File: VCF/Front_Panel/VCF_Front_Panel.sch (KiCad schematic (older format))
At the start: 1 part

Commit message: Bunch of bug fixes and tweaks
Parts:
- removed TP1: TestPoint, TestPoint:TestPoint_Pad_1.0x1.0mm, symbol Connector:TestPoint
- added H1: Top_MH, Eurorack:eurorack_mounting_hole, symbol Mechanical:MountingHole_Pad
- added H10: Res_Amt, Eurorack:pot_fp_hole, symbol Mechanical:MountingHole_Pad
- added H11: Res_Mod, Eurorack:jack_fp_hole, symbol Mechanical:MountingHole_Pad
- added H12: In_1, Eurorack:jack_fp_hole, symbol Mechanical:MountingHole_Pad
- added H13: In_2, Eurorack:jack_fp_hole, symbol Mechanical:MountingHole_Pad
- added H14: In_3, Eurorack:jack_fp_hole, symbol Mechanical:MountingHole_Pad
- added H15: Out, Eurorack:jack_fp_hole, symbol Mechanical:MountingHole_Pad
- added H2: Cutoff, Eurorack:pot_fp_hole, symbol Mechanical:MountingHole_Pad
- added H3: Cutoff_Amt, Eurorack:pot_fp_hole, symbol Mechanical:MountingHole_Pad
- added H4: Cutoff_Mod, Eurorack:jack_fp_hole, symbol Mechanical:MountingHole_Pad
- added H5: In_Amt_1, Eurorack:pot_fp_hole, symbol Mechanical:MountingHole_Pad
- added H6: In_Amt_2, Eurorack:pot_fp_hole, symbol Mechanical:MountingHole_Pad
- added H7: In_Amt_3, Eurorack:pot_fp_hole, symbol Mechanical:MountingHole_Pad
- added H8: Bottom_MH, Eurorack:eurorack_mounting_hole, symbol Mechanical:MountingHole_Pad
- added H9: Res, Eurorack:pot_fp_hole, symbol Mechanical:MountingHole_Pad
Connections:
- wire segments 2 -> 0

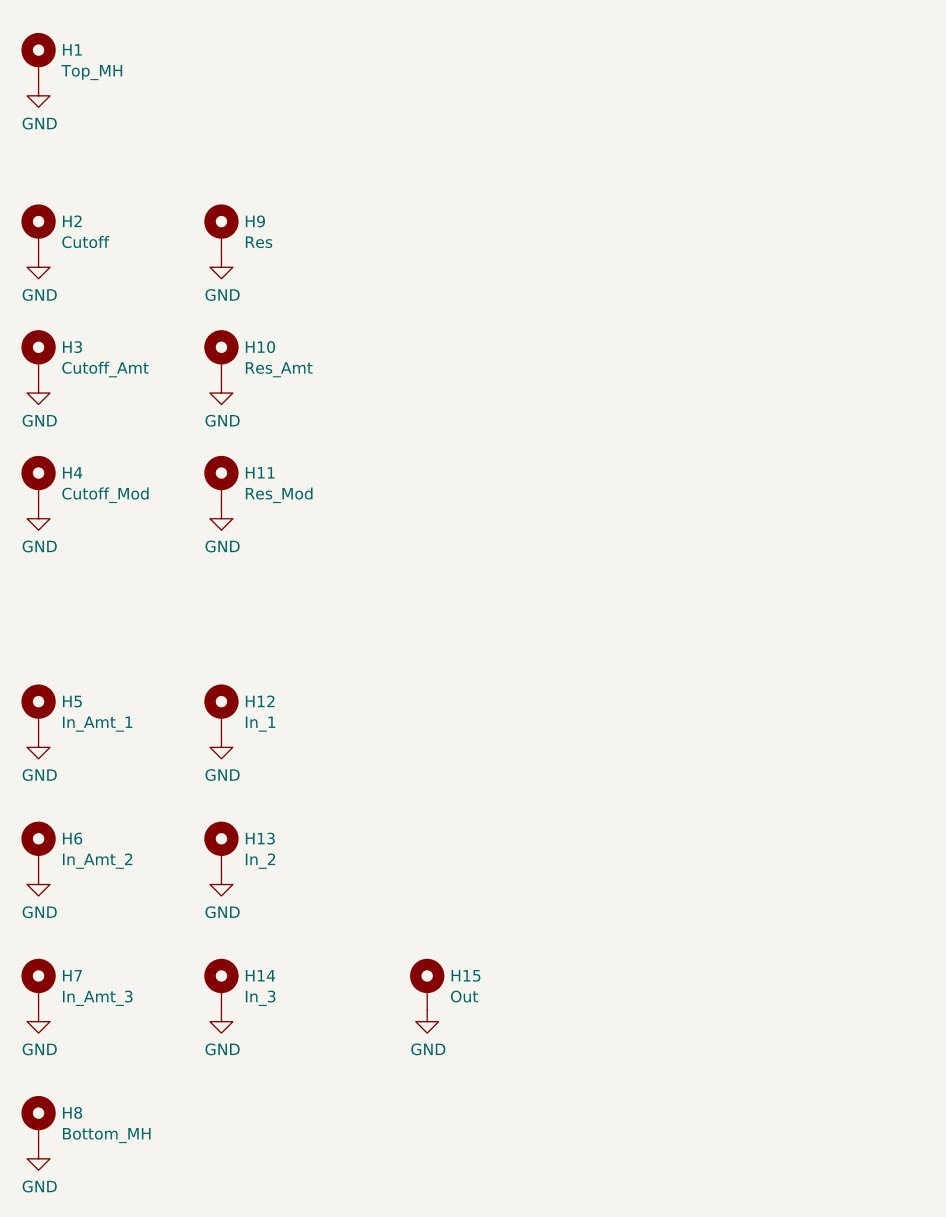
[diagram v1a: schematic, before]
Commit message: Make VCF front panel bigger. Re-align IO and FP boards.
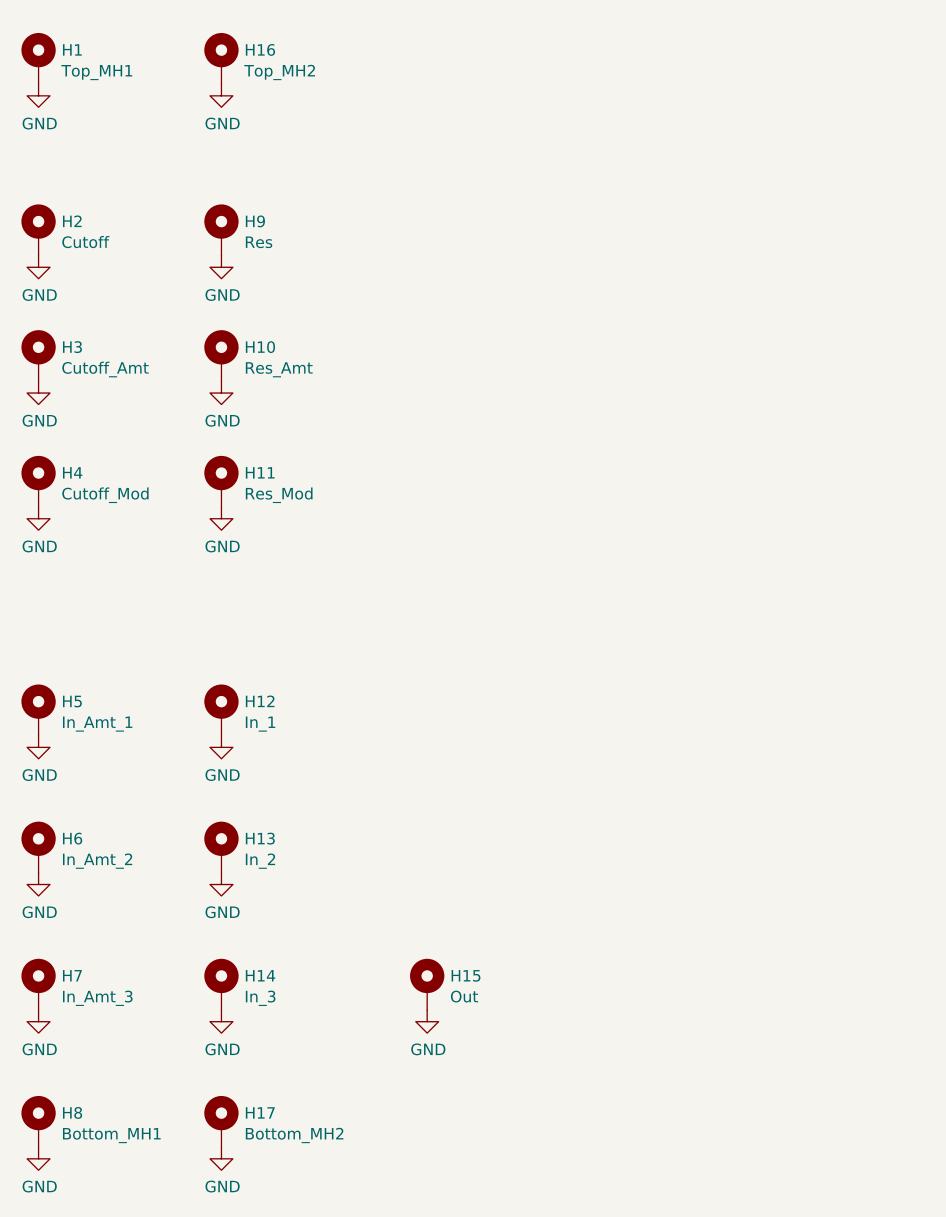
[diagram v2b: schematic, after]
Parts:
- added H16: Top_MH2, Eurorack:eurorack_mounting_hole, symbol Mechanical:MountingHole_Pad
- added H17: Bottom_MH2, Eurorack:eurorack_mounting_hole, symbol Mechanical:MountingHole_Pad
- H1: value Top_MH -> Top_MH1
- H8: value Bottom_MH -> Bottom_MH1
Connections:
- net GND: now also H16.1, H17.1
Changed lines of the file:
@@
 P 3650 1250
 F 0 "H1" H 3750 1299 50  0000 L CNN
-F 1 "Top_MH" H 3750 1208 50  0000 L CNN
+F 1 "Top_MH1" H 3750 1208 50  0000 L CNN
 F 2 "Eurorack:eurorack_mounting_hole" H 3650 1250 50  0001 C CNN
 F 3 "~" H 3650 1250 50  0001 C CNN
@@
 P 3650 5900
 F 0 "H8" H 3750 5949 50  0000 L CNN
-F 1 "Bottom_MH" H 3750 5858 50  0000 L CNN
+F 1 "Bottom_MH1" H 3750 5858 50  0000 L CNN
 F 2 "Eurorack:eurorack_mounting_hole" H 3650 5900 50  0001 C CNN
 F 3 "~" H 3650 5900 50  0001 C CNN
@@
 	1    0    0    -1
 $EndComp
+$Comp
+L Mechanical:MountingHole_Pad H16
+U 1 1 5D9BE294
+P 4450 1250
+F 0 "H16" H 4550 1299 50  0000 L CNN
+F 1 "Top_MH2" H 4550 1208 50  0000 L CNN
+F 2 "Eurorack:eurorack_mounting_hole" H 4450 1250 50  0001 C CNN
+F 3 "~" H 4450 1250 50  0001 C CNN
+	1    4450 1250
+	1    0    0    -1
+$EndComp
+$Comp
+L power:GND #PWR0116
+U 1 1 5D9BE29A
+P 4450 1350
+F 0 "#PWR0116" H 4450 1100 50  0001 C CNN
+F 1 "GND" H 4455 1177 50  0000 C CNN
+F 2 "" H 4450 1350 50  0001 C CNN
+F 3 "" H 4450 1350 50  0001 C CNN
+	1    4450 1350
+	1    0    0    -1
+$EndComp
+$Comp
+L Mechanical:MountingHole_Pad H17
+U 1 1 5D9BE9E4
+P 4450 5900
+F 0 "H17" H 4550 5949 50  0000 L CNN
+F 1 "Bottom_MH2" H 4550 5858 50  0000 L CNN
+F 2 "Eurorack:eurorack_mounting_hole" H 4450 5900 50  0001 C CNN
+F 3 "~" H 4450 5900 50  0001 C CNN
+	1    4450 5900
+	1    0    0    -1
+$EndComp
+$Comp
+L power:GND #PWR0117
+U 1 1 5D9BE9EA
+P 4450 6000
+F 0 "#PWR0117" H 4450 5750 50  0001 C CNN
+F 1 "GND" H 4455 5827 50  0000 C CNN
+F 2 "" H 4450 6000 50  0001 C CNN
+F 3 "" H 4450 6000 50  0001 C CNN
+	1    4450 6000
+	1    0    0    -1
+$EndComp
